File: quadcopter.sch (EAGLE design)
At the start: 65 parts, among them J1 AVR_SPI_PRG_6NS, U1 ATMEGA128RFA1, Y2 16MHz

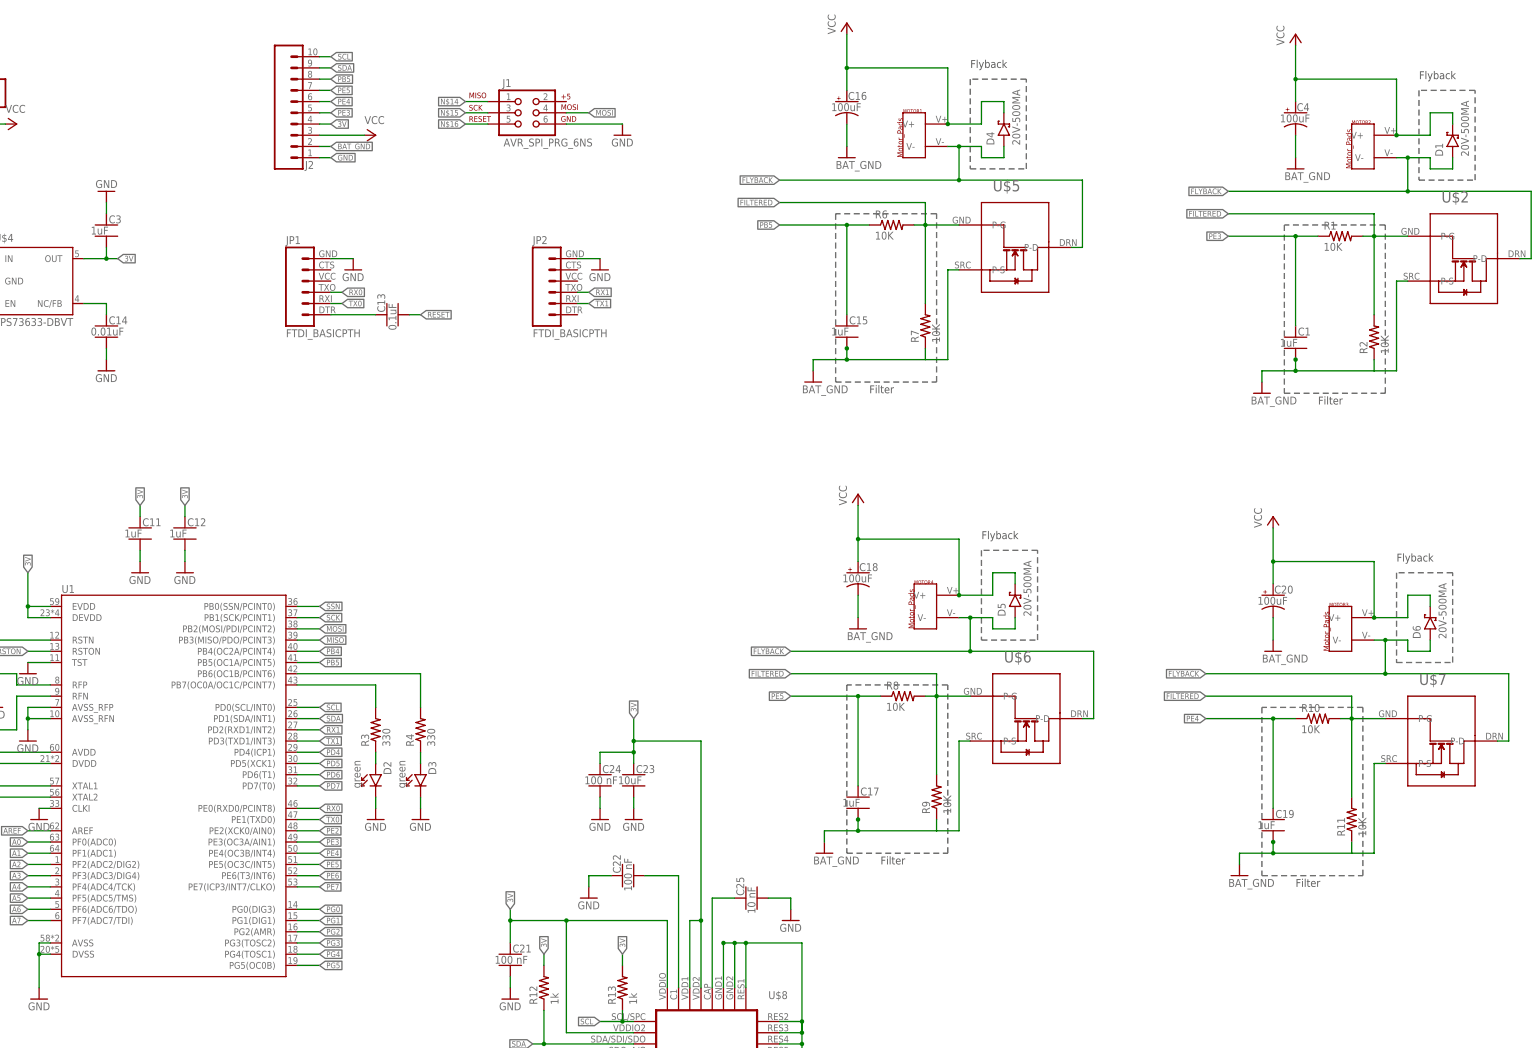
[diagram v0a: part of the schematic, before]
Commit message: Added LEDs, correct resistors, and replaced some devices with correct variants.
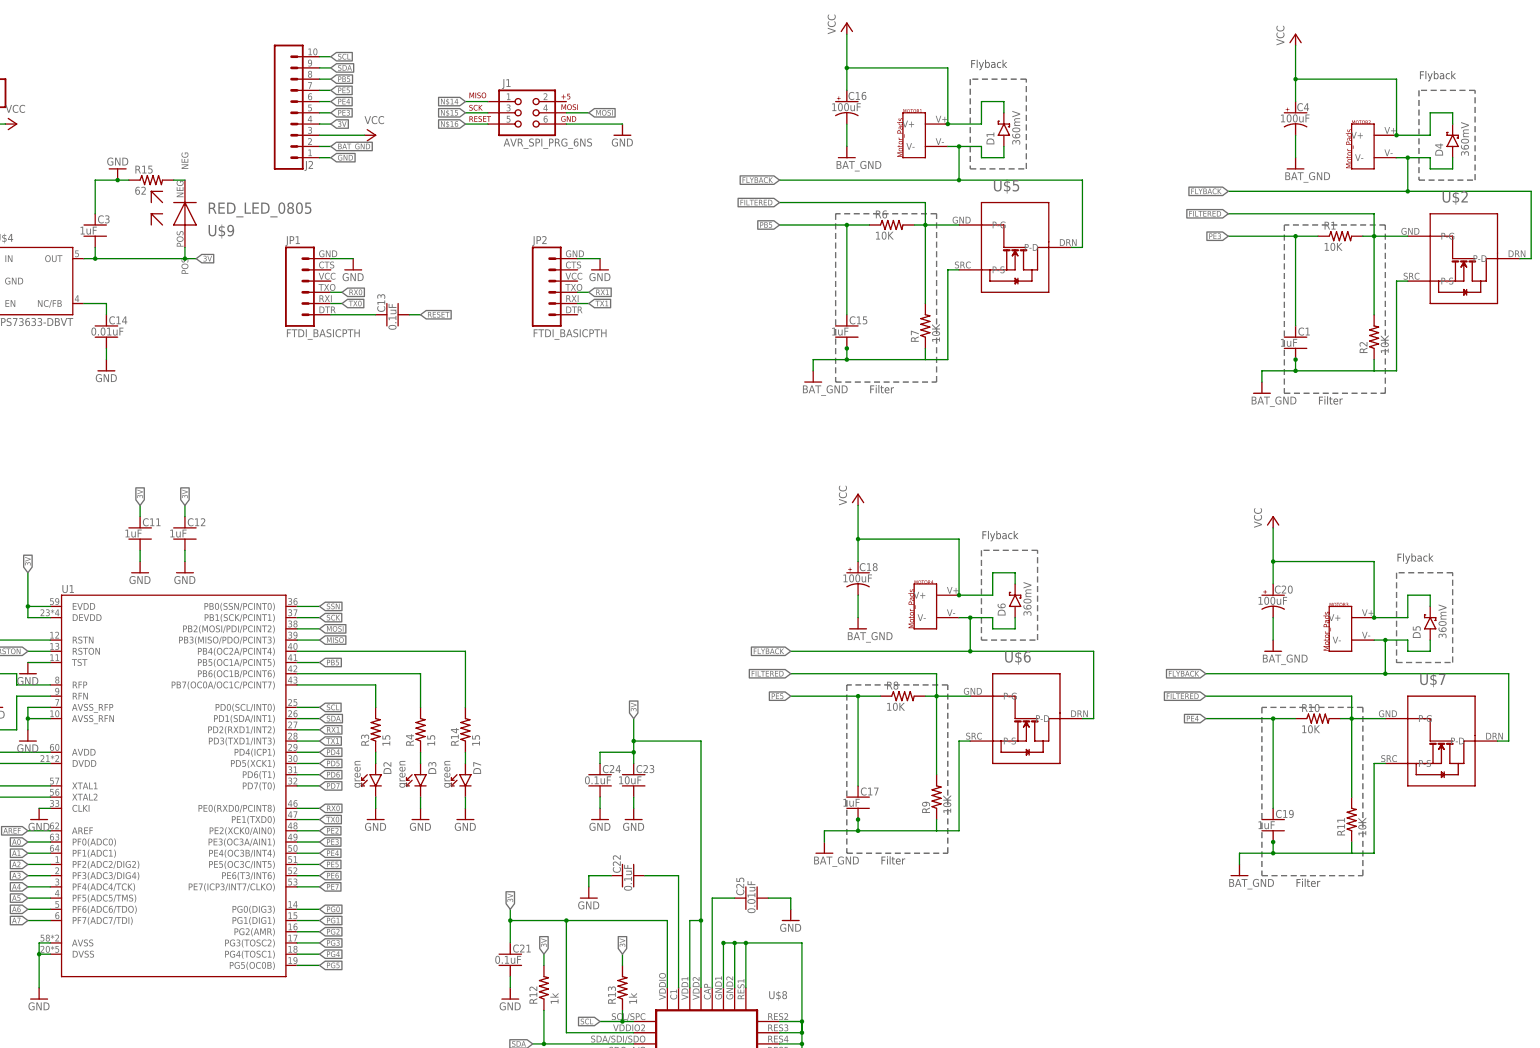
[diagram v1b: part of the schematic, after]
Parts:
- added D7: green, quadparts_prebuilt:DIODE-LED_SMD-2012-0805-GREEN
- added R14: 15, quadparts_prebuilt:RESISTOR_SMD-2012-0805-15
- added R15: 62, quadparts_prebuilt:RESISTOR_SMD-2012-0805-62
- added U$9: RED_LED_0805, LEDs:RED_LED_0805
- C21, C22, C24: value 100 nF -> 0.1uF; device quadparts_prebuilt:CAPACITOR-NP_SMD-2012-0805_CERAMIC -> quadparts_prebuilt:CAPACITOR-NP_SMD-2012-0805_CERAMIC-0.1UF
- C25: value 10 nF -> 0.01uF; device quadparts_prebuilt:CAPACITOR-NP_SMD-2012-0805_CERAMIC -> quadparts_prebuilt:CAPACITOR-NP_SMD-2012-0805_CERAMIC-0.01UF
- D1, D4, D5, D6: value 20V-500MA -> 360mV; device quadparts_prebuilt:DIODE-SCHOTTKY_SMD-SOD123 -> quadparts_prebuilt:DIODE-SCHOTTKY_SMD-SOD123-360MV
- R12, R13: device quadparts_prebuilt:RESISTOR_SMD-2012-0805 -> quadparts_prebuilt:RESISTOR_SMD-2012-0805-1K
- R3, R4: value 330 -> 15; device quadparts_prebuilt:RESISTOR_SMD-2012-0805-330 -> quadparts_prebuilt:RESISTOR_SMD-2012-0805-15
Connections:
- new net N$18: R15.2, U$9.NEG
- new net N$2: D7.A, R14.1
- net 3V: now also U$9.POS
- net GND: now also D7.C, R15.1
- net PB4: now also R14.2
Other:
- moved on the sheet: C3, D1, D4, D5, D6

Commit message: final commits for Lab 4
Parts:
- U$9: value RED_LED_0805 -> (none)
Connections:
- net 3V: no longer C16.+, C18.+, C20.+, C4.+, D1.C, D4.C, D5.C, D6.C, MOTOR1.V+, MOTOR2.V+, MOTOR3.V+, MOTOR4.V+
- net BAT_GND: now also C1.2, C15.2, C16.-, C17.2, C18.-, C19.2, C20.-, C4.-, R11.1, R2.1, R7.1, R9.1, U$2.P-S, U$5.P-S, U$6.P-S, U$7.P-S
- net GND: no longer C1.2, C15.2, C16.-, C17.2, C18.-, C19.2, C20.-, C4.-, R11.1, R2.1, R7.1, R9.1, U$2.P-S, U$5.P-S, U$6.P-S, U$7.P-S
- net VCC: now also C16.+, C18.+, C20.+, C4.+, D1.C, D4.C, D5.C, D6.C, MOTOR1.V+, MOTOR2.V+, MOTOR3.V+, MOTOR4.V+

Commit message: now, this is really the last commit because there was more to add and now there isn't
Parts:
- U$9: value (none) -> Red
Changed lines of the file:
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@@
 <part name="GND38" library="quadparts_prebuilt" deviceset="GND" device=""/>
 <part name="GND39" library="quadparts_prebuilt" deviceset="GND" device=""/>
-<part name="U$9" library="LEDs" deviceset="RED_LED_0805" device=""/>
+<part name="U$9" library="LEDs" deviceset="RED_LED_0805" device="" value="Red"/>
 <part name="D7" library="quadparts_prebuilt" deviceset="DIODE-LED_" device="SMD-2012-0805-GREEN" value="green"/>
 <part name="GND40" library="quadparts_prebuilt" deviceset="GND" device=""/>
